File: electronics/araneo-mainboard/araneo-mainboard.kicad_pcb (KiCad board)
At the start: 2 copper layers, 71.5 x 63.8 mm, 89 parts, among them IC1 TPS54302DDCR, IC2 BMI270, IC3 MMC5983MA, J2 OLED, J3 GPIO, SW2 SW, SW3 SW, U4 POWER, U5 PAM8403D, U6 3V3

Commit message: electronics: add credits
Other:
- board text added: "15.07.2026-08.08.2026 Projekt inżynierski prowadzony przez Mateusza Cholewińskiego Rev. 6"
- board text added: "Płytka zweryfikowana przez: Oliwier Woźniak Wojciech Szafrański"
- board text removed: "15.07.2026-04.08.2026 Projekt inżynierski prowadzony przez Mateusza Cholewińskiego"
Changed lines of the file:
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@@
 		)
 	)
-	(gr_text "15.07.2026-04.08.2026\nProjekt inżynierski\nprowadzony przez\nMateusza Cholewińskiego"
+	(gr_text "Płytka zweryfikowana przez:\nOliwier Woźniak\nWojciech Szafrański"
+		(at 98.5 72.5 90)
+		(layer "B.SilkS")
+		(effects
+			(font
+				(size 1 1)
+				(thickness 0.2)
+				(bold yes)
+			)
+			(justify left bottom mirror)
+		)
+	)
+	(gr_text "15.07.2026-08.08.2026\nProjekt inżynierski\nprowadzony przez\nMateusza Cholewińskiego\nRev. 6"
 		(at 136.5 57 90)
 		(layer "B.SilkS")

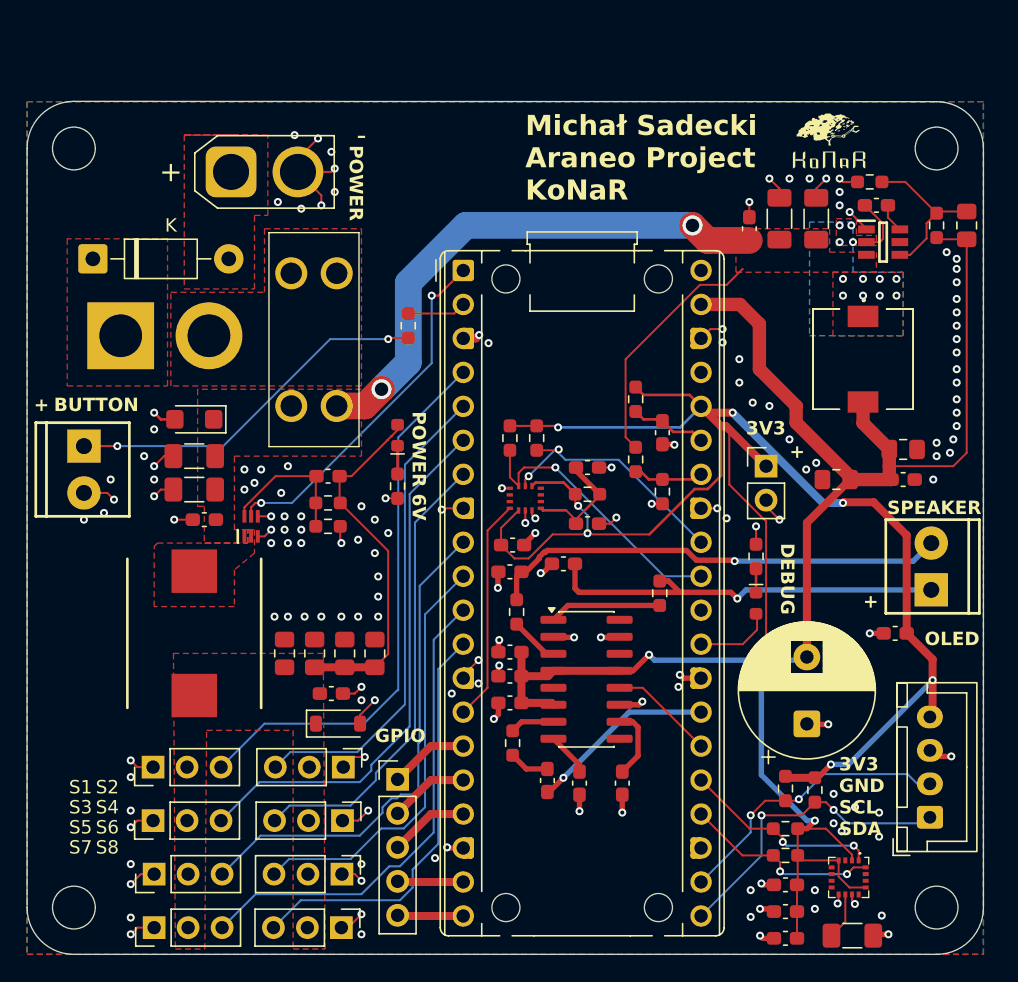
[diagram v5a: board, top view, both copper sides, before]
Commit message: electronics: change buck layout
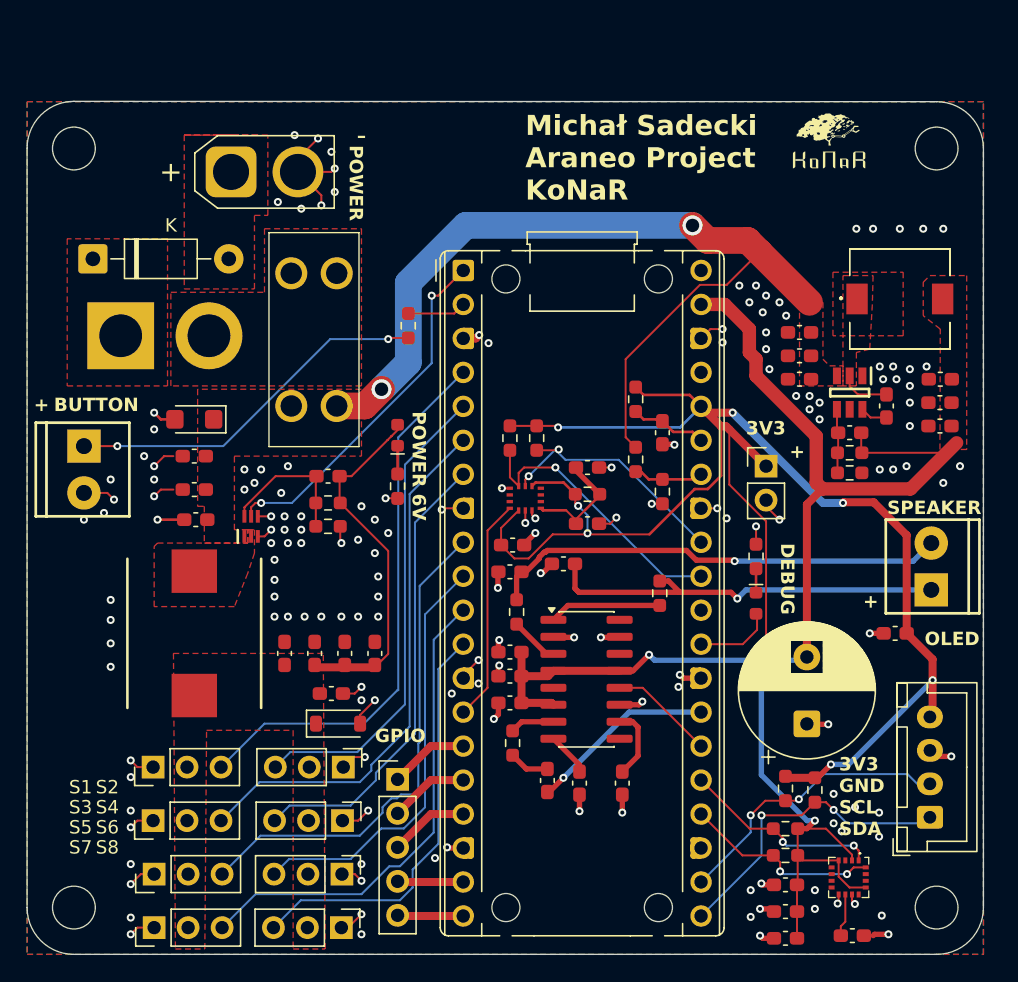
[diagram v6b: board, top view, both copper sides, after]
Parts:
- C2, C31, C32, C39, C40: footprint Capacitor_SMD:C_1206_3216Metric_Pad1.33x1.80mm_HandSolder -> Capacitor_SMD:C_0603_1608Metric_Pad1.08x0.95mm_HandSolder
- C29, C30, C34, C36, C37, C38: footprint Capacitor_SMD:C_0805_2012Metric_Pad1.18x1.45mm_HandSolder -> Capacitor_SMD:C_0603_1608Metric_Pad1.08x0.95mm_HandSolder
- C41: value 100p -> 75p; footprint Capacitor_SMD:C_0805_2012Metric_Pad1.18x1.45mm_HandSolder -> Capacitor_SMD:C_0603_1608Metric_Pad1.08x0.95mm_HandSolder
- CFF1: value 100nF -> 75p
- moved R17 21.8 mm to (153.0, 68.0), turned to 180 degrees
- moved R16 18.2 mm to (153.0, 66.5), turned to 0 degrees
- moved C41 17.8 mm to (153.0, 65.0), turned to 180 degrees
- moved C20 15.0 mm to (155.8, 63.0), turned to -90 degrees
- moved C40 12.1 mm to (149.2, 61.0), turned to 180 degrees
- moved IC1 11.5 mm to (153.0, 62.0), turned to -90 degrees
- moved C29 10.8 mm to (159.8, 61.0)
- moved C39 10.4 mm to (149.2, 59.2), turned to 180 degrees
- moved C35 8.61 mm to (149.2, 57.5), turned to 180 degrees
- moved C44 6.37 mm to (159.8, 62.8), turned to 0 degrees
- moved L2 5.27 mm to (156.8, 55.0), turned to 90 degrees
- moved C30 3.26 mm to (159.8, 64.5), turned to 180 degrees
- moved C33 0.64 mm to (104.1, 71.5)
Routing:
- net +5V: track 97.1 -> 79.3 mm
- net +7.4V_F: track 58.8 -> 67.0 mm
- net /FB5: track 12.1 -> 4.81 mm
- net GND: track 94.5 -> 87.6 mm, vias 156 -> 162
- net /SW5_L: track 4.42 -> 3.78 mm, vias 12 -> 0
- added copper zone on F.Cu, net +5V
- removed copper zone on B.Cu, net /SW5_L

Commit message: electronics: change 22u footprint
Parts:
- C29, C30, C36, C37, C38: footprint Capacitor_SMD:C_0603_1608Metric_Pad1.08x0.95mm_HandSolder -> Capacitor_SMD:C_0805_2012Metric_Pad1.18x1.45mm_HandSolder
- moved C30 0.50 mm to (159.8, 65.0)
- moved C44 0.25 mm to (159.8, 63.0)

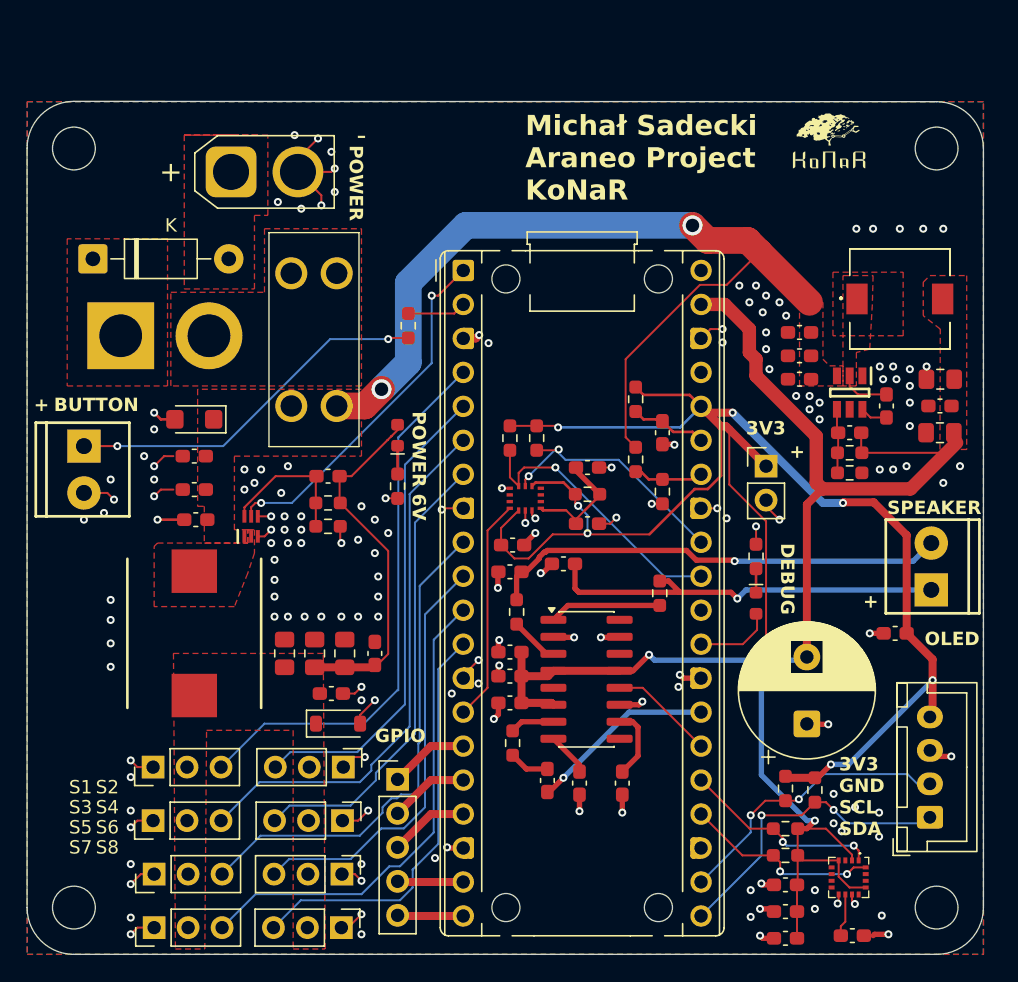
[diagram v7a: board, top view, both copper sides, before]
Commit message: electronics: move uC to have USB inlined with border
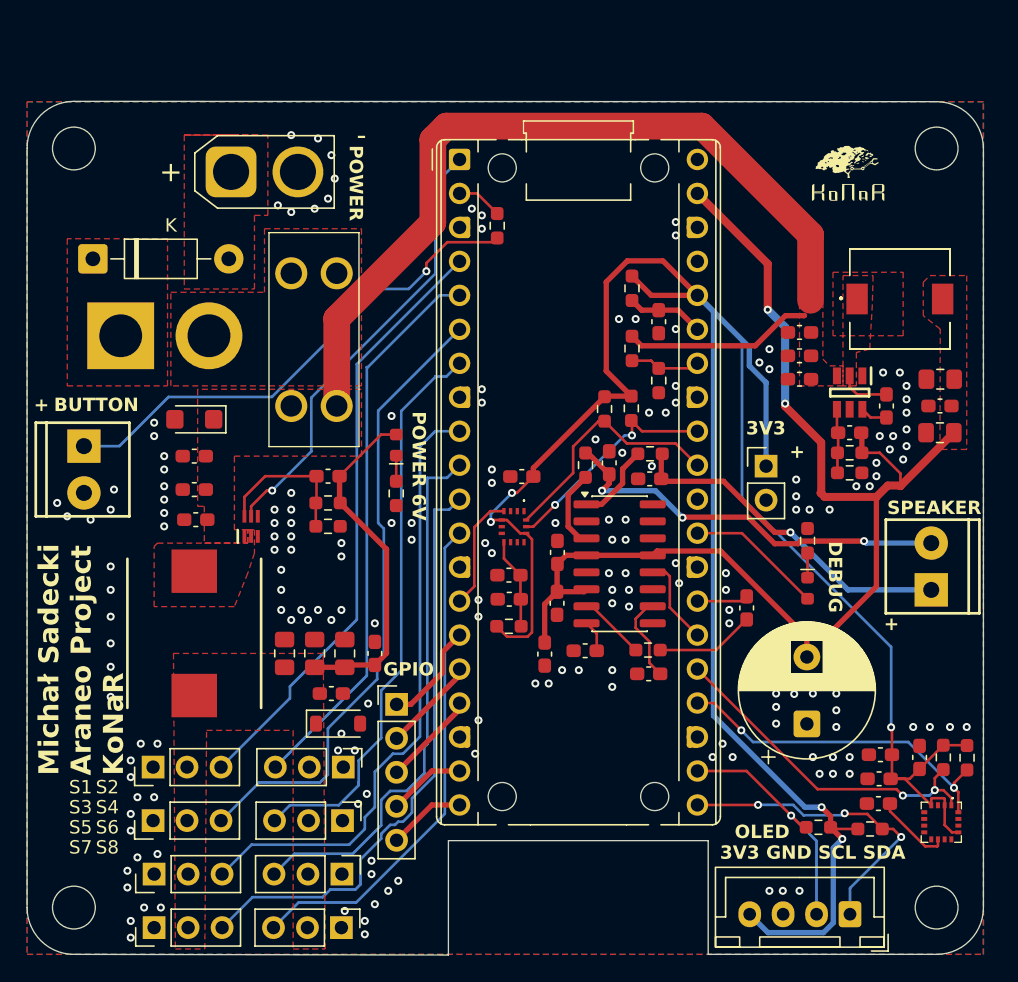
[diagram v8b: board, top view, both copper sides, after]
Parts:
- removed C19: 0.1uF, Capacitor_SMD:C_0603_1608Metric_Pad1.08x0.95mm_HandSolder
- moved C13 19.7 mm to (145.3, 78.1), turned to -90 degrees
- moved C5 16.8 mm to (158.2, 89.3), turned to -90 degrees
- moved R4 15.4 mm to (161.8, 89.3), turned to 90 degrees
- moved R3 12.9 mm to (160.0, 89.3), turned to 90 degrees
- moved R9 12.3 mm to (137.9, 81.2), turned to 180 degrees
- moved C4 12.1 mm to (155.2, 90.9)
- moved R21 12.1 mm to (133.2, 67.4)
- moved C3 12.0 mm to (155.3, 89.1)
- moved C15 11.8 mm to (131.2, 74.0), turned to 90 degrees
- moved FB4 11.5 mm to (127.5, 79.5)
- moved C42 11.5 mm to (127.5, 77.5), turned to 0 degrees
- moved C12 11.0 mm to (135.0, 67.2), turned to -90 degrees
- moved R20 10.5 mm to (138.1, 66.6), turned to 0 degrees
- moved C2 10.1 mm to (155.2, 92.7), turned to 180 degrees
- moved R14 10.0 mm to (126.7, 49.5)
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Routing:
- net GND: track 87.6 -> 0.00 mm, vias 162 -> 177
- net +3V3: track 162.9 -> 186.3 mm, vias 9 -> 5
- net /MAG_SCL: track 14.9 -> 25.7 mm
- net /MAG_SDA: track 14.8 -> 25.5 mm
- net +5V: track 79.3 -> 89.6 mm, vias 1 -> 2
- net /SPEAKER: track 14.0 -> 3.83 mm, vias 1 -> 0
- net /BTN_R: track 27.6 -> 37.7 mm, vias 2 -> 1
- net /PWM5: track 37.4 -> 46.2 mm
- net /PWM6: track 31.8 -> 40.4 mm
- net /PWM7: track 36.3 -> 44.6 mm
- net /PWM4: track 34.4 -> 42.5 mm
- net /IMU_INT1: track 16.7 -> 8.69 mm
- net +7.4V_F: track 67.0 -> 73.9 mm, vias 2 -> 0
- net /PWM3: track 40.3 -> 47.1 mm
- net /EN: track 26.8 -> 33.4 mm, vias 2 -> 1
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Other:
- outline, holes or cut-outs redrawn
